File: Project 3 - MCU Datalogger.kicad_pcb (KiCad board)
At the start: 2 copper layers, 2 parts

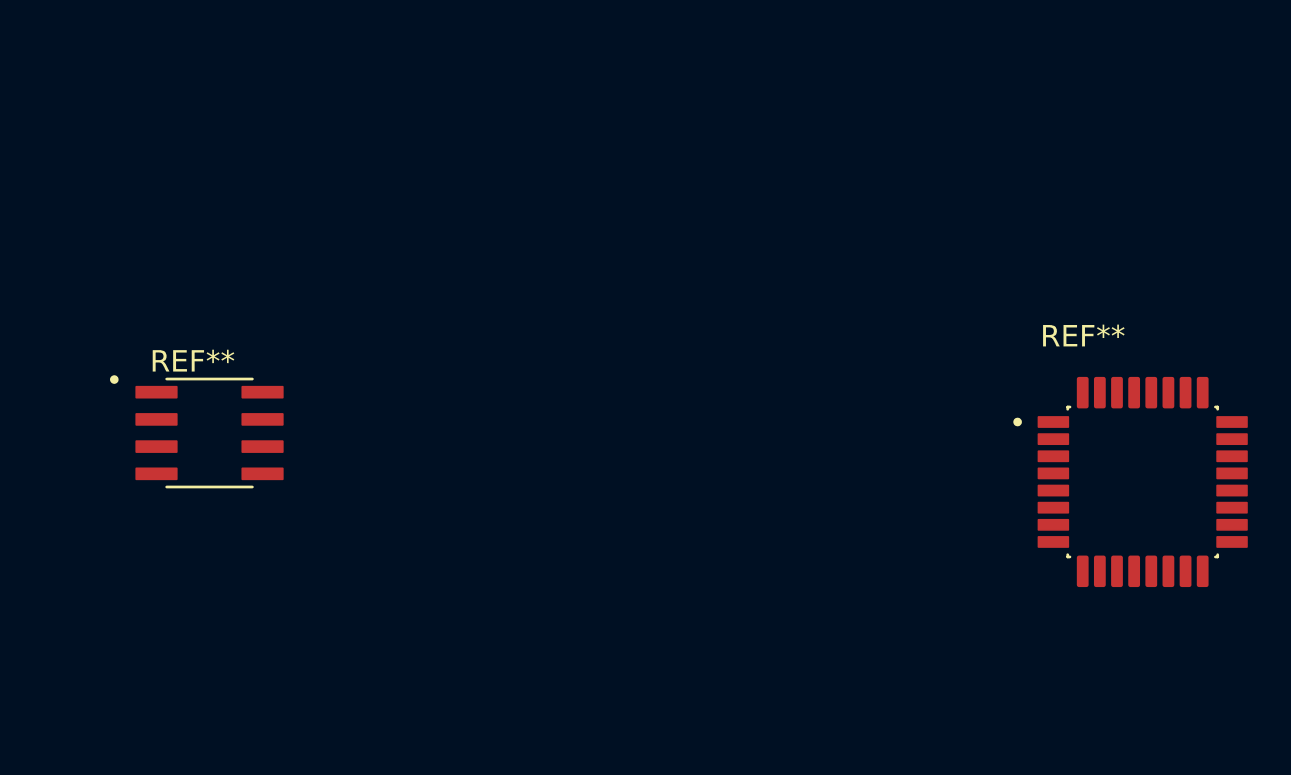
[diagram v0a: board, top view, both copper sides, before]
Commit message: Imported symbols into pcb new and updated power net class properties
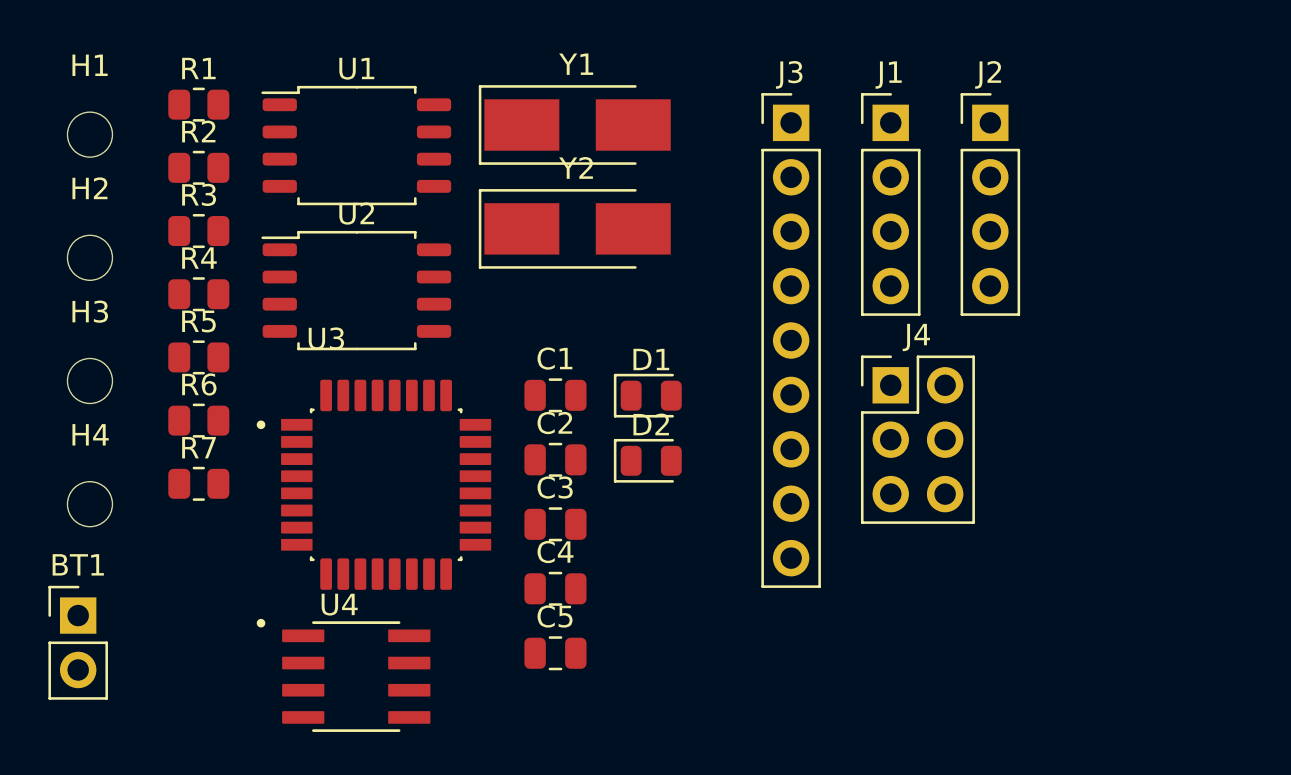
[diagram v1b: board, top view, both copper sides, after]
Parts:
- removed REF**: QFP80P900X900X120-32N, Datalogger Clock Footprints:QFP80P900X900X120-32N
- removed REF**: SOIC127P600X175-8N, Footprints:SOIC127P600X175-8N
- added BT1: Battery, Connector_PinHeader_2.54mm:PinHeader_1x02_P2.54mm_Vertical, F.Cu at (114.0, 82.7)
- added C1: 0.1uF, Capacitor_SMD:C_0805_2012Metric, F.Cu at (136.3, 72.4)
- added C2: 22pF, Capacitor_SMD:C_0805_2012Metric, F.Cu at (136.3, 75.4)
- added C3: 22pF, Capacitor_SMD:C_0805_2012Metric, F.Cu at (136.3, 78.4)
- added C4: 0.1uF, Capacitor_SMD:C_0805_2012Metric, F.Cu at (136.3, 81.4)
- added C5: 100nF, Capacitor_SMD:C_0805_2012Metric, F.Cu at (136.3, 84.5)
- added D1: LED, LED_SMD:LED_0805_2012Metric, F.Cu at (140.8, 72.4)
- added D2: LED, LED_SMD:LED_0805_2012Metric, F.Cu at (140.8, 75.5)
- added H1: MountingHole, MountingHole:MountingHole_2.1mm, F.Cu at (114.6, 60.2)
- added H2: MountingHole, MountingHole:MountingHole_2.1mm, F.Cu at (114.6, 66.0)
- added H3: MountingHole, MountingHole:MountingHole_2.1mm, F.Cu at (114.6, 71.7)
- added H4: MountingHole, MountingHole:MountingHole_2.1mm, F.Cu at (114.6, 77.5)
- added J1: Conn_01x04_Pin, Connector_PinHeader_2.54mm:PinHeader_1x04_P2.54mm_Vertical, F.Cu at (151.9, 59.7)
- added J2: Conn_01x04_Pin, Connector_PinHeader_2.54mm:PinHeader_1x04_P2.54mm_Vertical, F.Cu at (156.6, 59.7)
- added J3: Conn_01x09_Pin, Connector_PinHeader_2.54mm:PinHeader_1x09_P2.54mm_Vertical, F.Cu at (147.3, 59.7)
- added J4: Conn_02x03_Odd_Even, Connector_PinHeader_2.54mm:PinHeader_2x03_P2.54mm_Vertical, F.Cu at (151.9, 71.9)
- added R1: 10K, Resistor_SMD:R_0805_2012Metric, F.Cu at (119.6, 58.8)
- added R2: 4.7K, Resistor_SMD:R_0805_2012Metric, F.Cu at (119.6, 61.8)
- added R3: 4.7K, Resistor_SMD:R_0805_2012Metric, F.Cu at (119.6, 64.7)
- added R4: 330, Resistor_SMD:R_0805_2012Metric, F.Cu at (119.6, 67.7)
- added R5: 330, Resistor_SMD:R_0805_2012Metric, F.Cu at (119.6, 70.6)
- added R6: 10K, Resistor_SMD:R_0805_2012Metric, F.Cu at (119.6, 73.6)
- added R7: 10K, Resistor_SMD:R_0805_2012Metric, F.Cu at (119.6, 76.5)
- added U1: 24LC1025, Package_SO:SOIC-8_5.23x5.23mm_P1.27mm, F.Cu at (127.0, 60.8)
- added U2: 24LC1025, Package_SO:SOIC-8_5.23x5.23mm_P1.27mm, F.Cu at (127.0, 67.5)
- added U3: ATMEGA328P-AU, Datalogger Clock Footprints:QFP80P900X900X120-32N, F.Cu at (128.4, 76.6)
- added U4: DS1337S+, Datalogger Clock Footprints:SOIC127P600X175-8N, F.Cu at (127.0, 85.5)
- added Y1: 32.768 KHz, Crystal:Crystal_SMD_5032-2Pin_5.0x3.2mm_HandSoldering, F.Cu at (137.3, 59.8)
- added Y2: 16 MHz, Crystal:Crystal_SMD_5032-2Pin_5.0x3.2mm_HandSoldering, F.Cu at (137.3, 64.6)

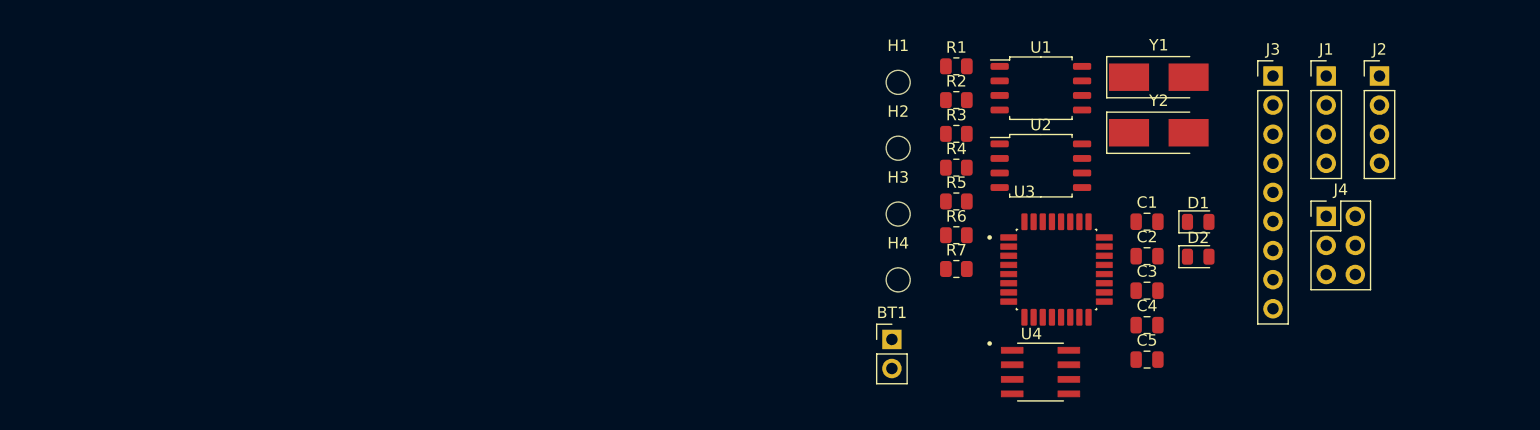
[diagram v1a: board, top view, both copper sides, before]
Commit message: placed footprints onto pcb design
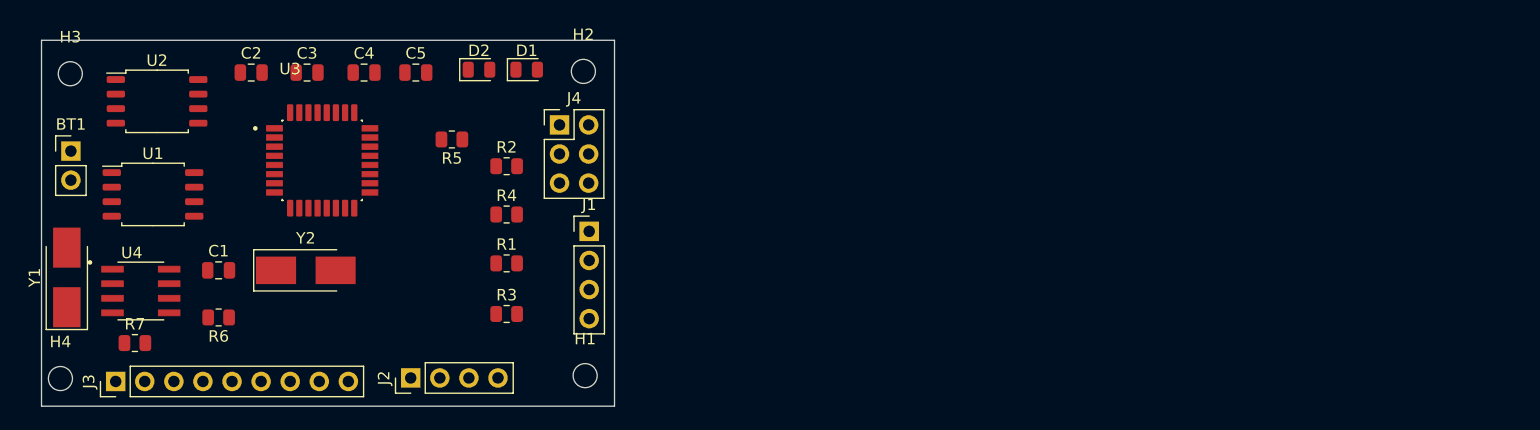
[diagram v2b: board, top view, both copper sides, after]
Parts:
- moved J3 104.5 mm to (46.2, 86.4), turned to 90 degrees
- moved Y1 97.0 mm to (42.0, 77.3), turned to 90 degrees
- moved J2 88.6 mm to (72.0, 86.1), turned to 90 degrees
- moved C1 81.2 mm to (55.2, 76.7)
- moved C2 79.9 mm to (58.1, 59.4)
- moved U4 78.9 mm to (48.4, 78.5)
- moved U1 78.1 mm to (49.5, 70.0)
- moved U2 77.4 mm to (49.8, 61.9)
- moved C3 75.8 mm to (62.9, 59.4)
- moved Y2 75.5 mm to (62.8, 76.7)
- moved H4 73.7 mm to (41.4, 86.1)
- moved BT1 73.6 mm to (42.3, 66.2)
- moved H3 73.3 mm to (42.3, 59.5)
- moved R7 72.0 mm to (47.9, 83.0)
- moved C4 71.8 mm to (67.9, 59.4)
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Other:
- board outline added: 50 x 32 mm

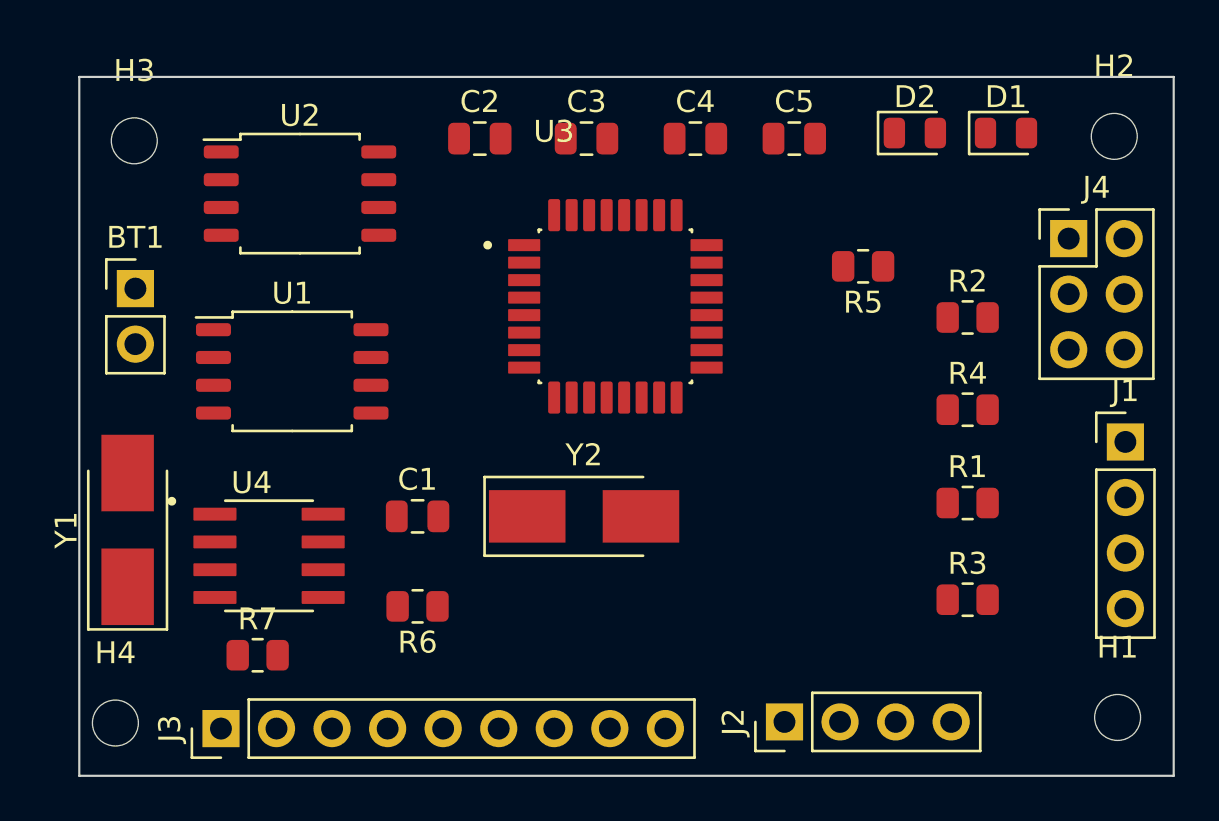
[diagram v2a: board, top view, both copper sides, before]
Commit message: wired 2 layer pcb
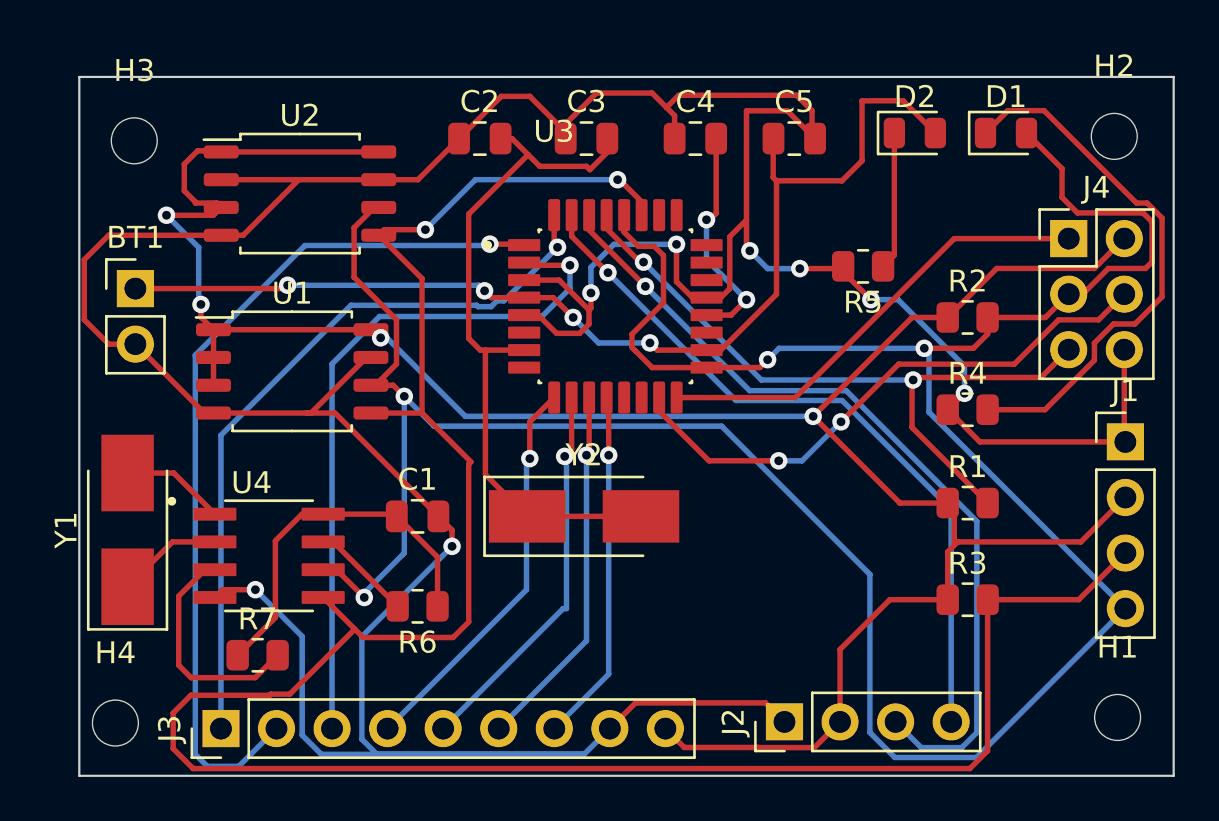
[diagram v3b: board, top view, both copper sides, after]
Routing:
- net GND: track 0.00 -> 188.1 mm, vias 0 -> 8
- net /SCK: track 0.00 -> 131.2 mm, vias 0 -> 4
- net /Vcc: track 0.00 -> 110.0 mm, vias 0 -> 4
- net /SDA: track 0.00 -> 107.2 mm, vias 0 -> 2
- net Net-(#FLG01-pwr): track 0.00 -> 49.8 mm, vias 0 -> 4
- net /D3: track 0.00 -> 40.1 mm, vias 0 -> 1
- net /RX: track 0.00 -> 38.1 mm, vias 0 -> 1
- net /D2: track 0.00 -> 33.9 mm, vias 0 -> 1
- net /TX: track 0.00 -> 33.2 mm, vias 0 -> 1
- net /RESET: track 0.00 -> 32.4 mm, vias 0 -> 2
- net Net-(U3-PB6): track 0.00 -> 32.3 mm
- net /D4: track 0.00 -> 32.2 mm, vias 0 -> 1
- net /MOSI: track 0.00 -> 26.0 mm, vias 0 -> 2
- net Net-(D1-K): track 0.00 -> 24.7 mm
- net /MISO: track 0.00 -> 20.9 mm
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
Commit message: fixed wiring violations and added silkscreen labels
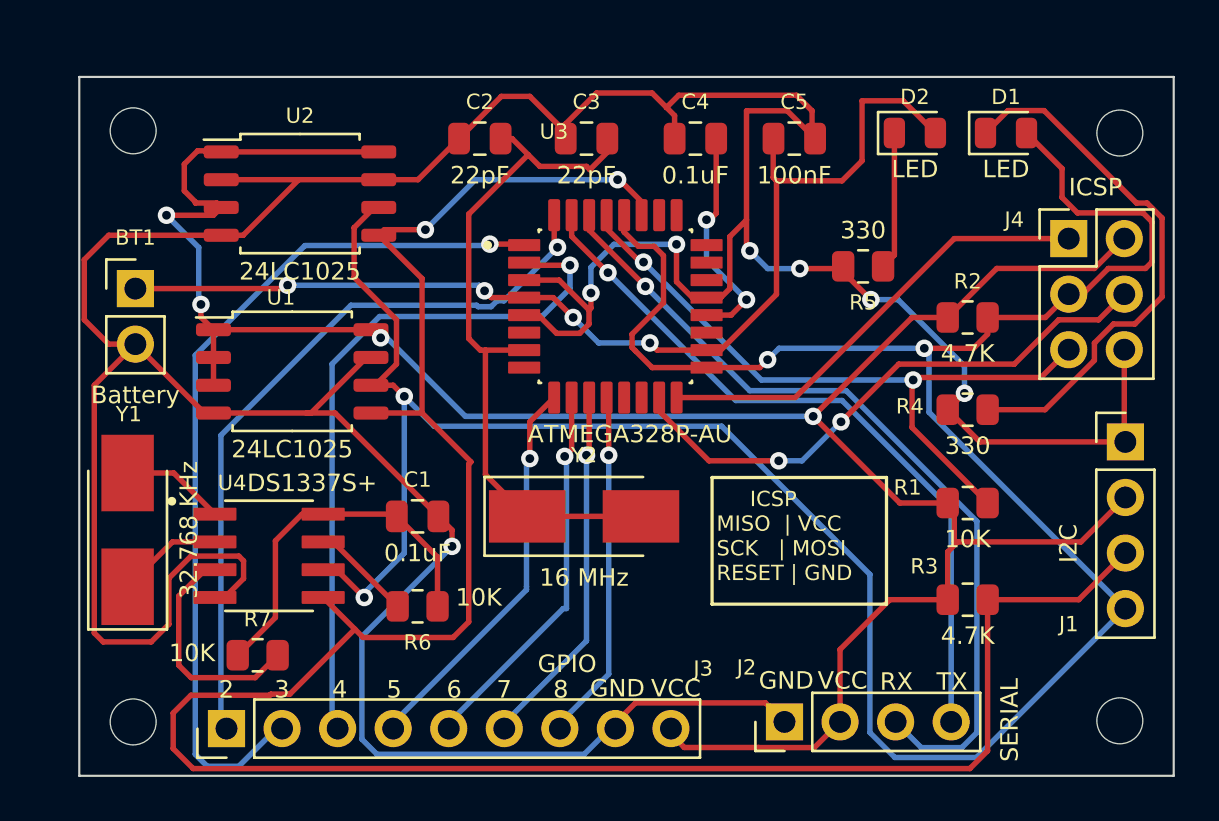
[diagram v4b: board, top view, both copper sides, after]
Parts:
- moved H4 0.81 mm to (42.2, 86.1)
- moved H3 0.46 mm to (42.2, 59.0)
- moved H2 0.30 mm to (87.3, 59.1)
- moved J3 0.25 mm to (46.5, 86.4)
- moved H1 0.18 mm to (87.3, 86.0)
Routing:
- net GND: track 188.1 -> 191.7 mm, vias 8 -> 7
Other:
- board text added: "2"
- board text added: "3"
- board text added: "4"
- board text added: "5"
- board text added: "6"
- board text added: "7"
- board text added: "8"
- board text added: "GND"
- board text added: "GPIO"
- board text added: "I2C"
- board text added: "ICSP"
- board text added: "ICSP MISO | VCC SCK | MOSI RESET | GND"
- board text added: "RX"
- board text added: "SERIAL"
- board text added: "TX"
- board text added: "VCC"

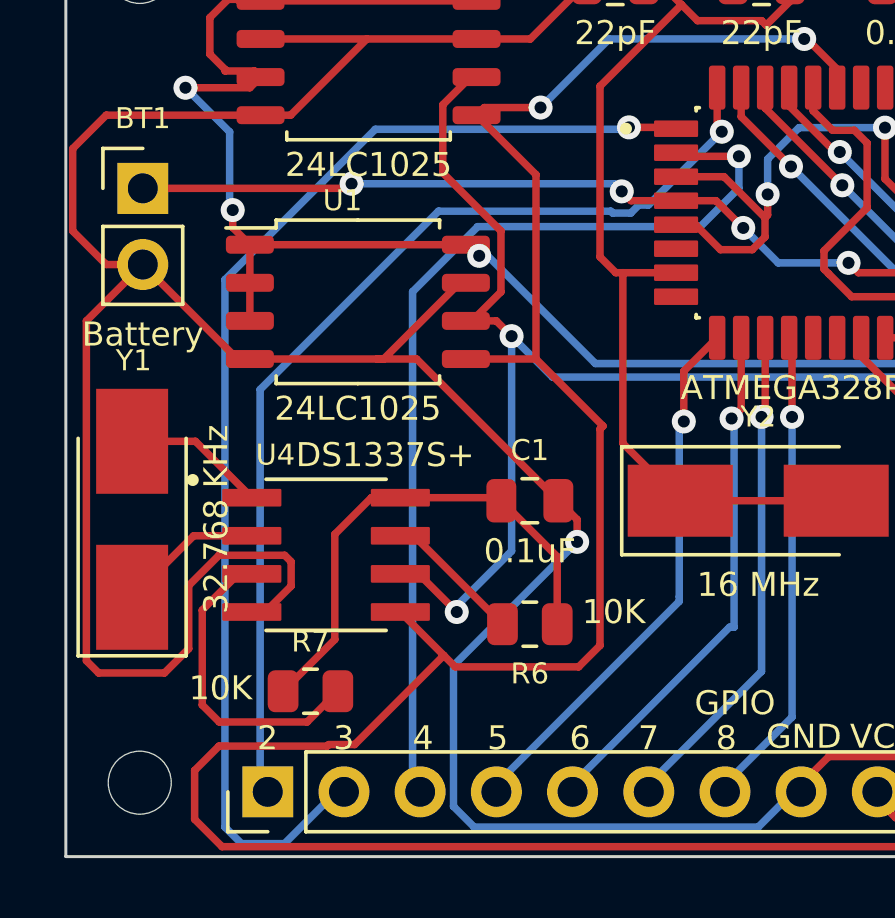
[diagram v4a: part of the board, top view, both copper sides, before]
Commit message: add board characteristics and 3d models
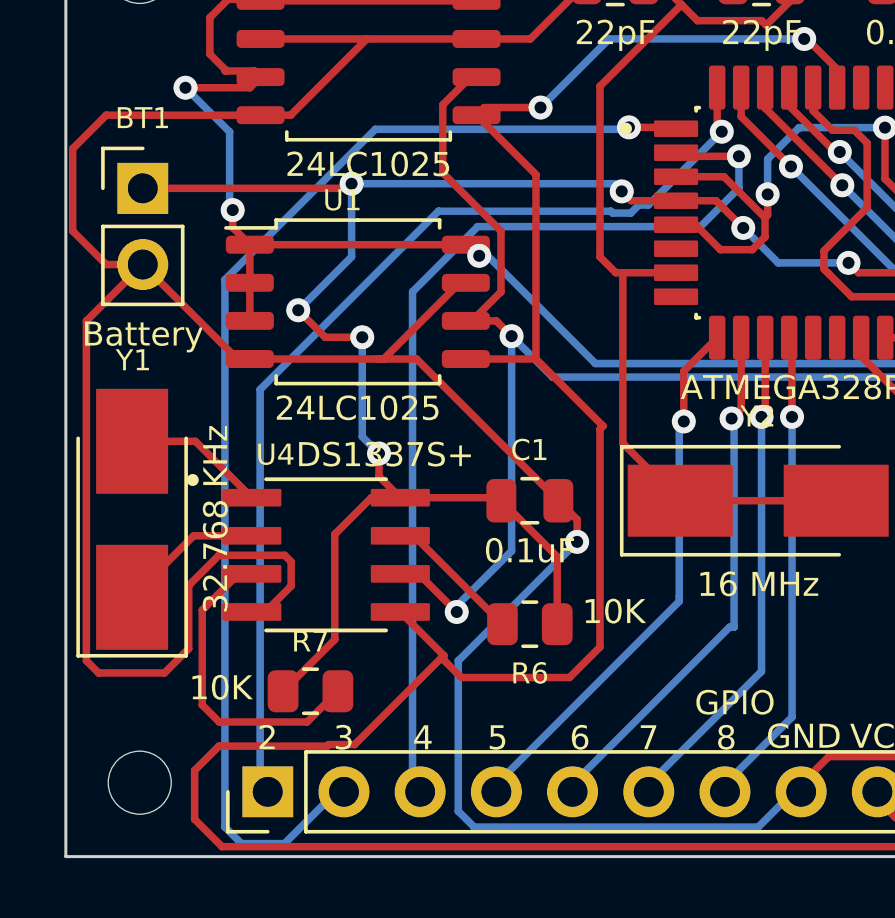
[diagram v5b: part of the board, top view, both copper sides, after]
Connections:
- BT1 pad 1: Net-(#FLG01-pwr) -> /VCC
- C1 pad 1: Net-(#FLG03-pwr) -> /VCC
- C5 pad 1: Net-(#FLG01-pwr) -> /VCC
- D2 pad 2: Net-(#FLG01-pwr) -> /VCC
- R6 pad 1: Net-(#FLG03-pwr) -> /VCC
- R7 pad 1: Net-(#FLG03-pwr) -> /VCC
- U3 pad 18: Net-(#FLG01-pwr) -> /VCC
- U3 pad 4: Net-(#FLG01-pwr) -> /VCC
- U4 pad 8: Net-(#FLG03-pwr) -> /VCC
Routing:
- net /VCC: track 0.00 -> 80.1 mm, vias 0 -> 7
- net Net-(#FLG01-pwr): track 49.8 -> 0.00 mm, vias 4 -> 0
- net Net-(#FLG03-pwr): track 16.9 -> 0.00 mm
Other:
- board text added: "0.0000 mm / 0.0000 mm"
- board text added: "0.3000 mm"
- board text added: "1.6000 mm"
- board text added: "50.0380 mm x 31.9532 mm"
- board text added: "BOARD CHARACTERISTICS"
- board text added: "Board Thickness:"
- board text added: "Board overall dimensions:"
- board text added: "Castellated pads:"
- board text added: "Copper Finish:"
- board text added: "Copper Layer Count:"
- board text added: "Edge card connectors:"
- board text added: "Impedance Control:"
- board text added: "Min hole diameter:"
- board text added: "Min track/spacing:"
- board text added: "No"
- board text added: "None"
- board text added: "Plated Board Edge:"
